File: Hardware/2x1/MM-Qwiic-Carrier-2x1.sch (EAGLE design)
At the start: 52 parts, among them J15 MICROMOD-2222-C, J2 QWIIC_RIGHT_ANGLE, J5 Vertical Qwiic Connector, U1 MCP73831, U5 AP7361C-33FGEUDFN-8

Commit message: Run of engineering checklist
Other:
- note added: "LiPo Range: 3.6-4.2V"
- note added: "v10"
- note removed: "v01"
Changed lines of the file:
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@@
 <text x="342.9" y="17.78" size="2.54" layer="94" font="vector">MM-Qwiic-Carrier-2x1</text>
 <text x="142.24" y="238.76" size="2.54" layer="94" font="vector" align="center">LED</text>
-<text x="419.1" y="7.62" size="2.54" layer="94" font="vector">v01</text>
+<text x="419.1" y="7.62" size="2.54" layer="94" font="vector">v10</text>
 <text x="132.08" y="167.64" size="1.778" layer="97" font="vector">Cut this jumper to
 remove power LED.</text>
@@
 <text x="368.3" y="236.22" size="1.778" layer="97" font="vector">Cut this jumper and use the PTH
 holes to measure current draw</text>
+<text x="292.1" y="165.1" size="1.778" layer="97" font="vector">LiPo Range: 3.6-4.2V</text>
 </plain>
 <instances>

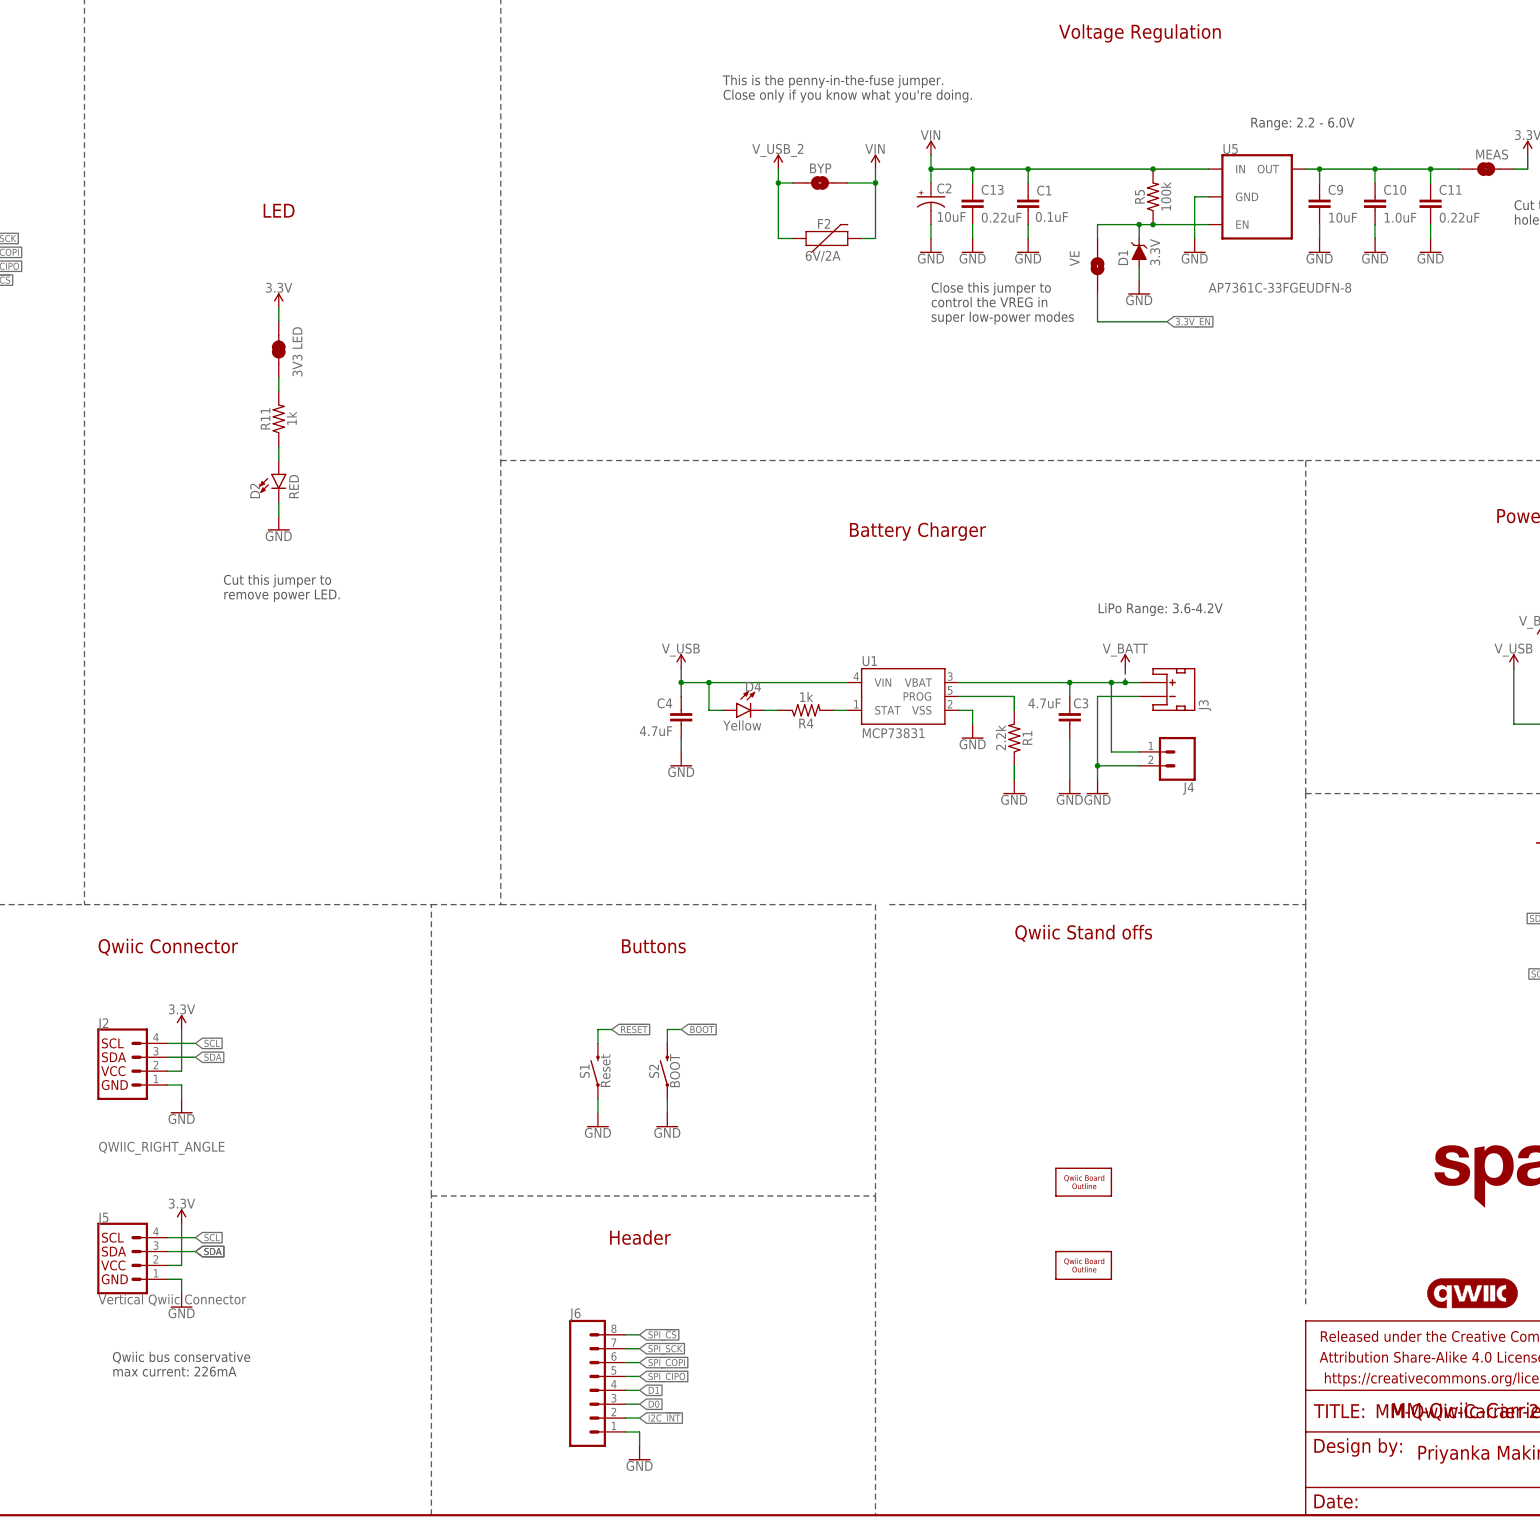
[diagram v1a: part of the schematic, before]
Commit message: Silk changes from red board design review
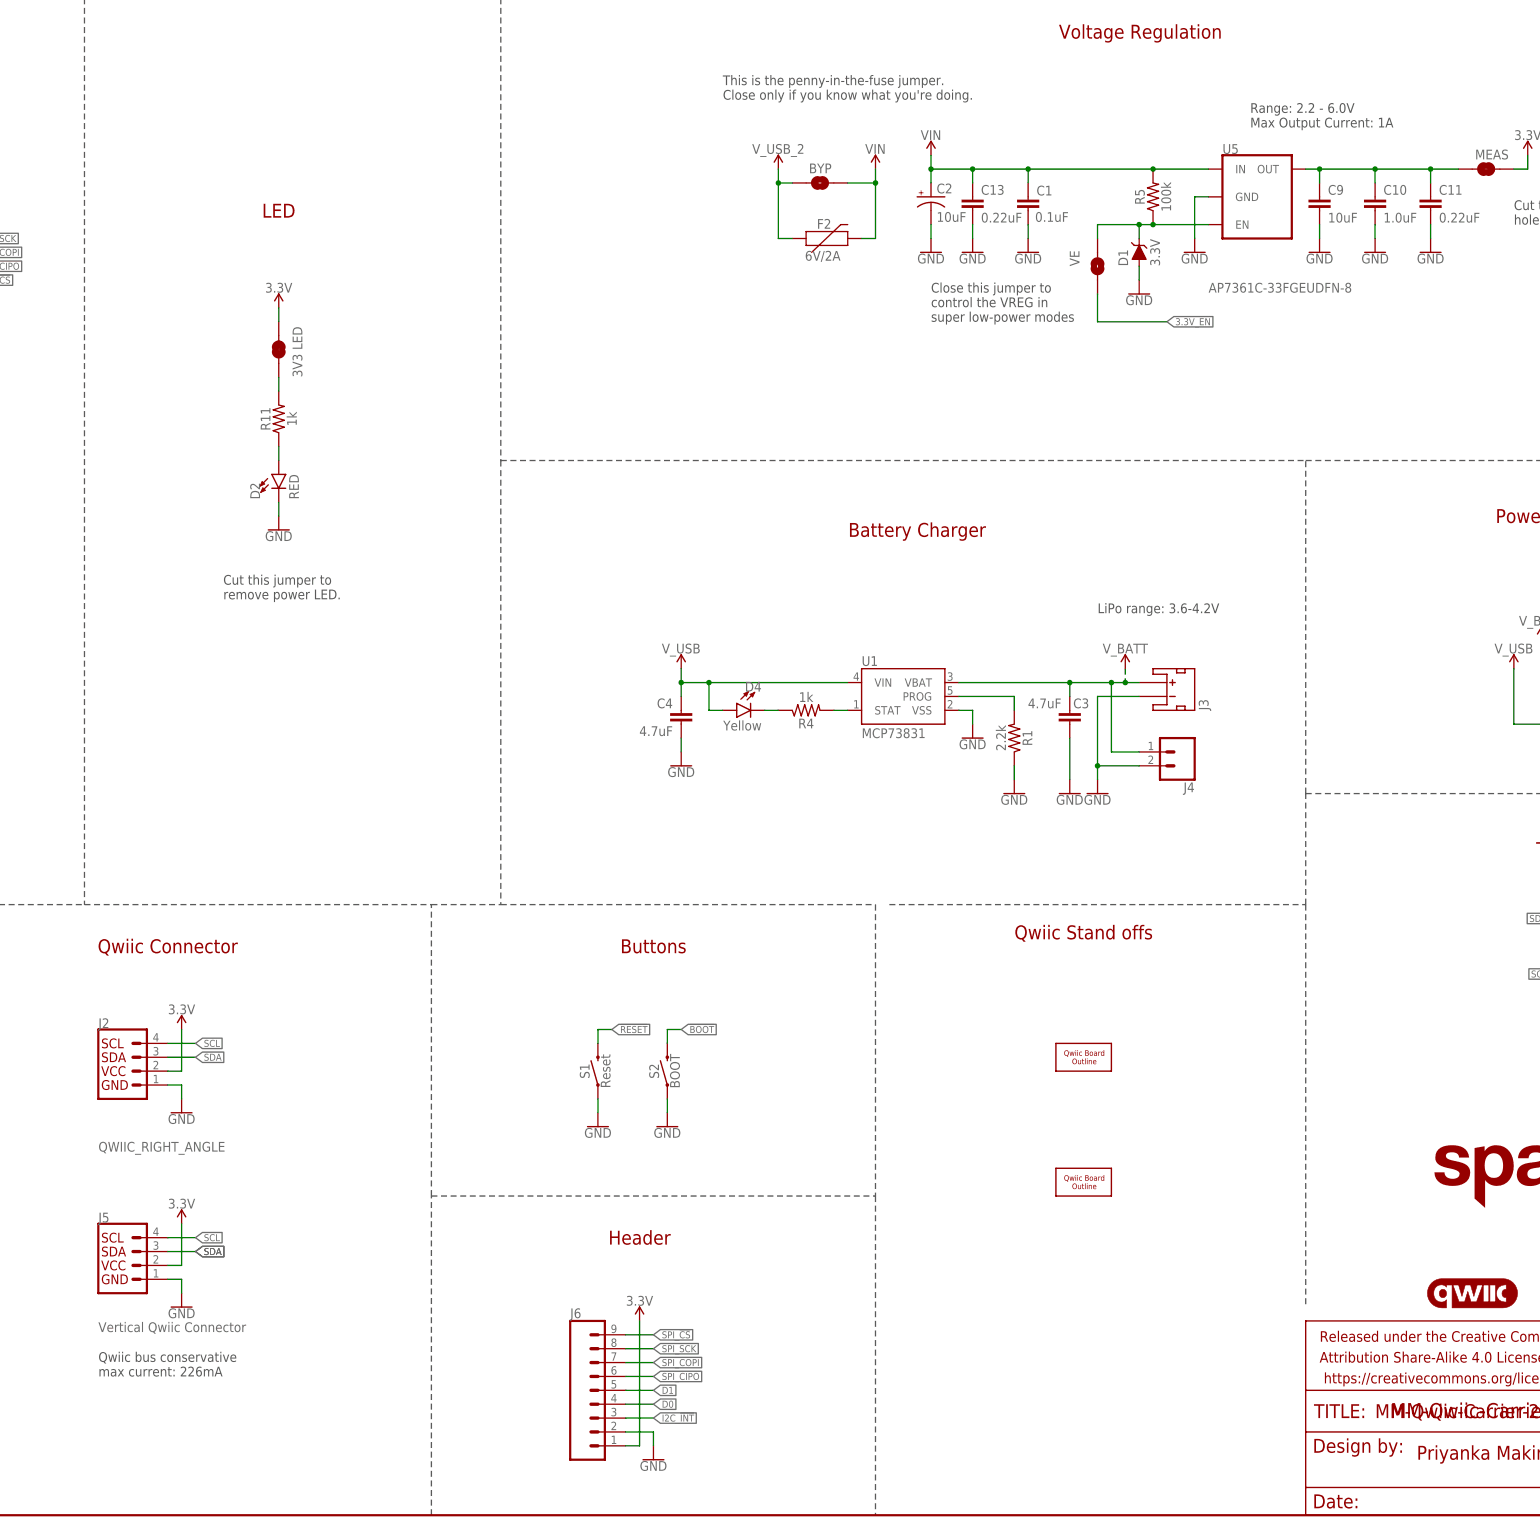
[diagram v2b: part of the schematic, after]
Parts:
- removed U$30: QWIIC_BOARD_OUTLINESTANDOFF, SparkFun-Boards:QWIIC_BOARD_OUTLINESTANDOFF
- added U$2: QWIIC_BOARD_OUTLINESTANDOFF, SparkFun-Boards:QWIIC_BOARD_OUTLINESTANDOFF
- J6: device SparkFun-Connectors:CONN_08NO_SILK_FEMALE_PTH -> SparkFun-Connectors:CONN_09NO_SILK
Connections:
- net 3.3V: now also J6.1
- net D0: now also J6.4; no longer J6.3
- net D1: now also J6.5; no longer J6.4
- net GND: now also J6.2; no longer J6.1
- net I2C_!INT!: now also J6.3; no longer J6.2
- net SPI_!CS!: now also J6.9; no longer J6.8
- net SPI_CIPO: now also J6.6; no longer J6.5
- net SPI_COPI: now also J6.7; no longer J6.6
- net SPI_SCK: now also J6.8; no longer J6.7
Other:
- note added: "LiPo range: 3.6-4.2V"
- note added: "Range: 2.2 - 6.0V Max Output Current: 1A"
- note removed: "LiPo Range: 3.6-4.2V"
- note removed: "Range: 2.2 - 6.0V"
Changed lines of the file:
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@@
 <?xml version="1.0" encoding="utf-8"?>
 <!DOCTYPE eagle SYSTEM "eagle.dtd">
-<eagle version="9.5.2">
+<eagle version="9.6.2">
 <drawing>
 <settings>
@@
 <part name="GND18" library="SparkFun-PowerSymbols" deviceset="GND" device=""/>
 <part name="SUPPLY14" library="SparkFun-PowerSymbols" deviceset="3.3V" device=""/>
-<part name="J6" library="SparkFun-Connectors" deviceset="CONN_08" device="NO_SILK_FEMALE_PTH"/>
 <part name="GND26" library="SparkFun-PowerSymbols" deviceset="GND" device=""/>
 <part name="U$5" library="SparkFun-Boards" deviceset="QWIIC_BOARD_OUTLINE" device="STANDOFF"/>
 <part name="SUPPLY15" library="SparkFun-PowerSymbols" deviceset="V_USB_2" device=""/>
 <part name="SUPPLY16" library="SparkFun-PowerSymbols" deviceset="V_USB_2" device=""/>
-<part name="U$30" library="SparkFun-Boards" deviceset="QWIIC_BOARD_OUTLINE" device="STANDOFF"/>
+<part name="J6" library="SparkFun-Connectors" deviceset="CONN_09" device="NO_SILK"/>
+<part name="SUPPLY17" library="SparkFun-PowerSymbols" deviceset="3.3V" device=""/>
+<part name="U$2" library="SparkFun-Boards" deviceset="QWIIC_BOARD_OUTLINE" device="STANDOFF"/>
 </parts>
 <sheets>
@@
 <text x="38.1" y="76.2" size="1.9304" layer="97" font="vector">Range: 4.2 - 5.2V</text>
 <text x="299.974" y="271.526" size="2.54" layer="94" font="vector" align="center">Voltage Regulation</text>
-<text x="320.04" y="254" size="1.778" layer="97" font="vector">Range: 2.2 - 6.0V</text>
+<text x="320.04" y="254" size="1.778" layer="97" font="vector">Range: 2.2 - 6.0V
+Max Output Current: 1A</text>
 <text x="261.62" y="218.44" size="1.778" layer="97" font="vector">Close this jumper to
 control the VREG in
@@
 <text x="381" y="182.88" size="2.54" layer="94" font="vector" align="center">Power Source Select</text>
 <text x="381" y="121.92" size="2.54" layer="94" font="vector" align="center">Test Points</text>
-<text x="111.76" y="25.4" size="1.778" layer="97" font="vector">Qwiic bus conservative
+<text x="109.22" y="25.4" size="1.778" layer="97" font="vector">Qwiic bus conservative
 max current: 226mA</text>
 <wire x1="170.18" y1="58.42" x2="251.46" y2="58.42" width="0.2032" layer="97" style="longdash"/>
@@
 <text x="368.3" y="236.22" size="1.778" layer="97" font="vector">Cut this jumper and use the PTH
 holes to measure current draw</text>
-<text x="292.1" y="165.1" size="1.778" layer="97" font="vector">LiPo Range: 3.6-4.2V</text>
+<text x="292.1" y="165.1" size="1.778" layer="97" font="vector">LiPo range: 3.6-4.2V</text>
 </plain>
 <instances>
@@
 </instance>
 <instance part="J5" gate="G$1" x="114.3" y="45.72" smashed="yes">
-<attribute name="VALUE" x="109.22" y="40.386" size="1.778" layer="96" font="vector" align="top-left"/>
+<attribute name="VALUE" x="109.22" y="35.306" size="1.778" layer="96" font="vector" align="top-left"/>
 <attribute name="NAME" x="109.22" y="53.594" size="1.778" layer="95" font="vector"/>
 </instance>
@@
 <attribute name="VALUE" x="124.46" y="56.134" size="1.778" layer="96" align="bottom-center"/>
 </instance>
-<instance part="J6" gate="G$1" x="200.66" y="22.86" smashed="yes">
-<attribute name="VALUE" x="195.58" y="10.414" size="1.778" layer="96" font="vector"/>
-<attribute name="NAME" x="195.58" y="36.068" size="1.778" layer="95" font="vector"/>
-</instance>
-<instance part="GND26" gate="1" x="208.28" y="10.16" smashed="yes">
-<attribute name="VALUE" x="208.28" y="9.906" size="1.778" layer="96" align="top-center"/>
+<instance part="GND26" gate="1" x="210.82" y="10.16" smashed="yes">
+<attribute name="VALUE" x="210.82" y="9.906" size="1.778" layer="96" align="top-center"/>
 </instance>
 <instance part="U$5" gate="G$1" x="289.56" y="60.96" smashed="yes"/>
@@
 <attribute name="VALUE" x="233.68" y="249.174" size="1.778" layer="96" align="bottom-center"/>
 </instance>
-<instance part="U$30" gate="G$1" x="289.56" y="45.72" smashed="yes"/>
+<instance part="J6" gate="J1" x="195.58" y="22.86" smashed="yes">
+<attribute name="VALUE" x="195.58" y="7.874" size="1.778" layer="96" font="vector"/>
+<attribute name="NAME" x="195.58" y="36.068" size="1.778" layer="95" font="vector"/>
+</instance>
+<instance part="SUPPLY17" gate="G$1" x="208.28" y="35.56" smashed="yes">
+<attribute name="VALUE" x="208.28" y="38.354" size="1.778" layer="96" align="bottom-center"/>
+</instance>
+<instance part="U$2" gate="G$1" x="289.56" y="83.82" smashed="yes"/>
 </instances>
 <busses>
@@
 </segment>
 <segment>
-<pinref part="J6" gate="G$1" pin="1"/>
-<wire x1="205.74" y1="15.24" x2="208.28" y2="15.24" width="0.1524" layer="91"/>
-<wire x1="208.28" y1="15.24" x2="208.28" y2="12.7" width="0.1524" layer="91"/>
+<wire x1="205.74" y1="15.24" x2="210.82" y2="15.24" width="0.1524" layer="91"/>
+<wire x1="210.82" y1="15.24" x2="210.82" y2="12.7" width="0.1524" layer="91"/>
 <pinref part="GND26" gate="1" pin="GND"/>
+<pinref part="J6" gate="J1" pin="2"/>
 </segment>
 </net>
@@
 <wire x1="124.46" y1="45.72" x2="124.46" y2="53.34" width="0.1524" layer="91"/>
 <pinref part="SUPPLY14" gate="G$1" pin="3.3V"/>
+</segment>
+<segment>
+<pinref part="J6" gate="J1" pin="1"/>
+<wire x1="205.74" y1="12.7" x2="208.28" y2="12.7" width="0.1524" layer="91"/>
+<wire x1="208.28" y1="12.7" x2="208.28" y2="35.56" width="0.1524" layer="91"/>
+<pinref part="SUPPLY17" gate="G$1" pin="3.3V"/>
 </segment>
 </net>
@@
 <net name="I2C_!INT!" class="0">
 <segment>
-<pinref part="J6" gate="G$1" pin="2"/>
-<wire x1="205.74" y1="17.78" x2="208.28" y2="17.78" width="0.1524" layer="91"/>
-<label x="208.28" y="17.78" size="1.27" layer="95" xref="yes"/>
+<wire x1="205.74" y1="17.78" x2="210.82" y2="17.78" width="0.1524" layer="91"/>
+<label x="210.82" y="17.78" size="1.27" layer="95" xref="yes"/>
+<pinref part="J6" gate="J1" pin="3"/>
 </segment>
 <segment>
@@
 <net name="D0" class="0">
 <segment>
-<pinref part="J6" gate="G$1" pin="3"/>
-<wire x1="205.74" y1="20.32" x2="208.28" y2="20.32" width="0.1524" layer="91"/>
-<label x="208.28" y="20.32" size="1.27" layer="95" xref="yes"/>
+<wire x1="205.74" y1="20.32" x2="210.82" y2="20.32" width="0.1524" layer="91"/>
+<label x="210.82" y="20.32" size="1.27" layer="95" xref="yes"/>
+<pinref part="J6" gate="J1" pin="4"/>
 </segment>
 <segment>
@@
 <net name="D1" class="0">
 <segment>
-<pinref part="J6" gate="G$1" pin="4"/>
-<wire x1="205.74" y1="22.86" x2="208.28" y2="22.86" width="0.1524" layer="91"/>
-<label x="208.28" y="22.86" size="1.27" layer="95" xref="yes"/>
+<wire x1="205.74" y1="22.86" x2="210.82" y2="22.86" width="0.1524" layer="91"/>
+<label x="210.82" y="22.86" size="1.27" layer="95" xref="yes"/>
+<pinref part="J6" gate="J1" pin="5"/>
 </segment>
 <segment>
@@
 <net name="SPI_SCK" class="0">
 <segment>
-<pinref part="J6" gate="G$1" pin="7"/>
-<wire x1="205.74" y1="30.48" x2="208.28" y2="30.48" width="0.1524" layer="91"/>
-<label x="208.28" y="30.48" size="1.27" layer="95" xref="yes"/>
+<wire x1="205.74" y1="30.48" x2="210.82" y2="30.48" width="0.1524" layer="91"/>
+<label x="210.82" y="30.48" size="1.27" layer="95" xref="yes"/>
+<pinref part="J6" gate="J1" pin="8"/>
 </segment>
 <segment>
@@
 <net name="SPI_!CS!" class="0">
 <segment>
-<pinref part="J6" gate="G$1" pin="8"/>
-<wire x1="205.74" y1="33.02" x2="208.28" y2="33.02" width="0.1524" layer="91"/>
-<label x="208.28" y="33.02" size="1.27" layer="95" xref="yes"/>
+<wire x1="205.74" y1="33.02" x2="210.82" y2="33.02" width="0.1524" layer="91"/>
+<label x="210.82" y="33.02" size="1.27" layer="95" xref="yes"/>
+<pinref part="J6" gate="J1" pin="9"/>
 </segment>
 <segment>
@@
 </segment>
 <segment>
-<pinref part="J6" gate="G$1" pin="6"/>
-<wire x1="205.74" y1="27.94" x2="208.28" y2="27.94" width="0.1524" layer="91"/>
-<label x="208.28" y="27.94" size="1.27" layer="95" xref="yes"/>
+<wire x1="205.74" y1="27.94" x2="210.82" y2="27.94" width="0.1524" layer="91"/>
+<label x="210.82" y="27.94" size="1.27" layer="95" xref="yes"/>
+<pinref part="J6" gate="J1" pin="7"/>
 </segment>
 </net>
@@
 </segment>
 <segment>
-<pinref part="J6" gate="G$1" pin="5"/>
-<wire x1="205.74" y1="25.4" x2="208.28" y2="25.4" width="0.1524" layer="91"/>
-<label x="208.28" y="25.4" size="1.27" layer="95" xref="yes"/>
-</segment>
-</net>
+<wire x1="205.74" y1="25.4" x2="210.82" y2="25.4" width="0.1524" layer="91"/>
+<label x="210.82" y="25.4" size="1.27" layer="95" xref="yes"/>
+<pinref part="J6" gate="J1" pin="6"/>
+</segment>
+</net>
